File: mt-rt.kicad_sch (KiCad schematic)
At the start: 0 parts

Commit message: added MCU
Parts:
- added U?: nRF52820-QDxx, Package_DFN_QFN:QFN-40-1EP_5x5mm_P0.4mm_EP3.6x3.6mm, symbol MCU_Nordic:nRF52820-QDxx
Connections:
- new net: U?.37 (VSS), U?.41 (VSS)
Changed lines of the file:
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@@
 		(comment 2 "Copyright (c) 2025 MiraTherm")
+	)
+	(symbol
+		(lib_id "MCU_Nordic:nRF52820-QDxx")
+		(at 127 80.01 0)
+		(unit 1)
+		(exclude_from_sim no)
+		(in_bom yes)
+		(on_board yes)
+		(dnp no)
+		(fields_autoplaced yes)
+		(property "Reference" "U?"
+			(at 129.1433 105.41 0)
+			(effects
+				(font
+					(size 1.27 1.27)
+				)
+				(justify left)
+			)
+		)
+		(property "Value" "nRF52820-QDxx"
+			(at 129.1433 107.95 0)
+			(effects
+				(font
+					(size 1.27 1.27)
+				)
+				(justify left)
+			)
+		)
+		(property "Footprint" "Package_DFN_QFN:QFN-40-1EP_5x5mm_P0.4mm_EP3.6x3.6mm"
+			(at 127 115.57 0)
+			(effects
+				(font
+					(size 1.27 1.27)
+				)
+				(hide yes)
+			)
+		)
+		(property "Datasheet" "https://infocenter.nordicsemi.com/pdf/nRF52820_PS_v1.0.pdf"
+			(at 110.49 31.75 0)
+			(effects
+				(font
+					(size 1.27 1.27)
+				)
+				(hide yes)
+			)
+		)
+		(property "Description" "Multiprotocol BLE/ANT/2.4 GHz/802.15.4 Cortex-M4 SoC, QFN-40"
+			(at 127 80.01 0)
+			(effects
+				(font
+					(size 1.27 1.27)
+				)
+				(hide yes)
+			)
+		)
+		(pin "28"
+		)
+		(pin "29"
+		)
+		(pin "24"
+		)
+		(pin "21"
+		)
+		(pin "12"
+		)
+		(pin "22"
+		)
+		(pin "13"
+		)
+		(pin "16"
+		)
+		(pin "27"
+		)
+		(pin "26"
+		)
+		(pin "41"
+		)
+		(pin "39"
+		)
+		(pin "2"
+		)
+		(pin "37"
+		)
+		(pin "9"
+		)
+		(pin "36"
+		)
+		(pin "5"
+		)
+		(pin "6"
+		)
+		(pin "7"
+		)
+		(pin "14"
+		)
+		(pin "15"
+		)
+		(pin "38"
+		)
+		(pin "20"
+		)
+		(pin "1"
+		)
+		(pin "8"
+		)
+		(pin "3"
+		)
+		(pin "23"
+		)
+		(pin "17"
+		)
+		(pin "32"
+		)
+		(pin "4"
+		)
+		(pin "19"
+		)
+		(pin "18"
+		)
+		(pin "25"
+		)
+		(pin "35"
+		)
+		(pin "11"
+		)
+		(pin "30"
+		)
+		(pin "10"
+		)
+		(pin "40"
+		)
+		(pin "31"
+		)
+		(pin "34"
+		)
+		(pin "33"
+		)
+		(instances
+			(project ""
+				(path "/ee47f507-02e8-4ef5-a6d4-1ac4b2022b93"
+					(reference "U?")
+					(unit 1)
+				)
+			)
+		)
 	)
 	(sheet_instances

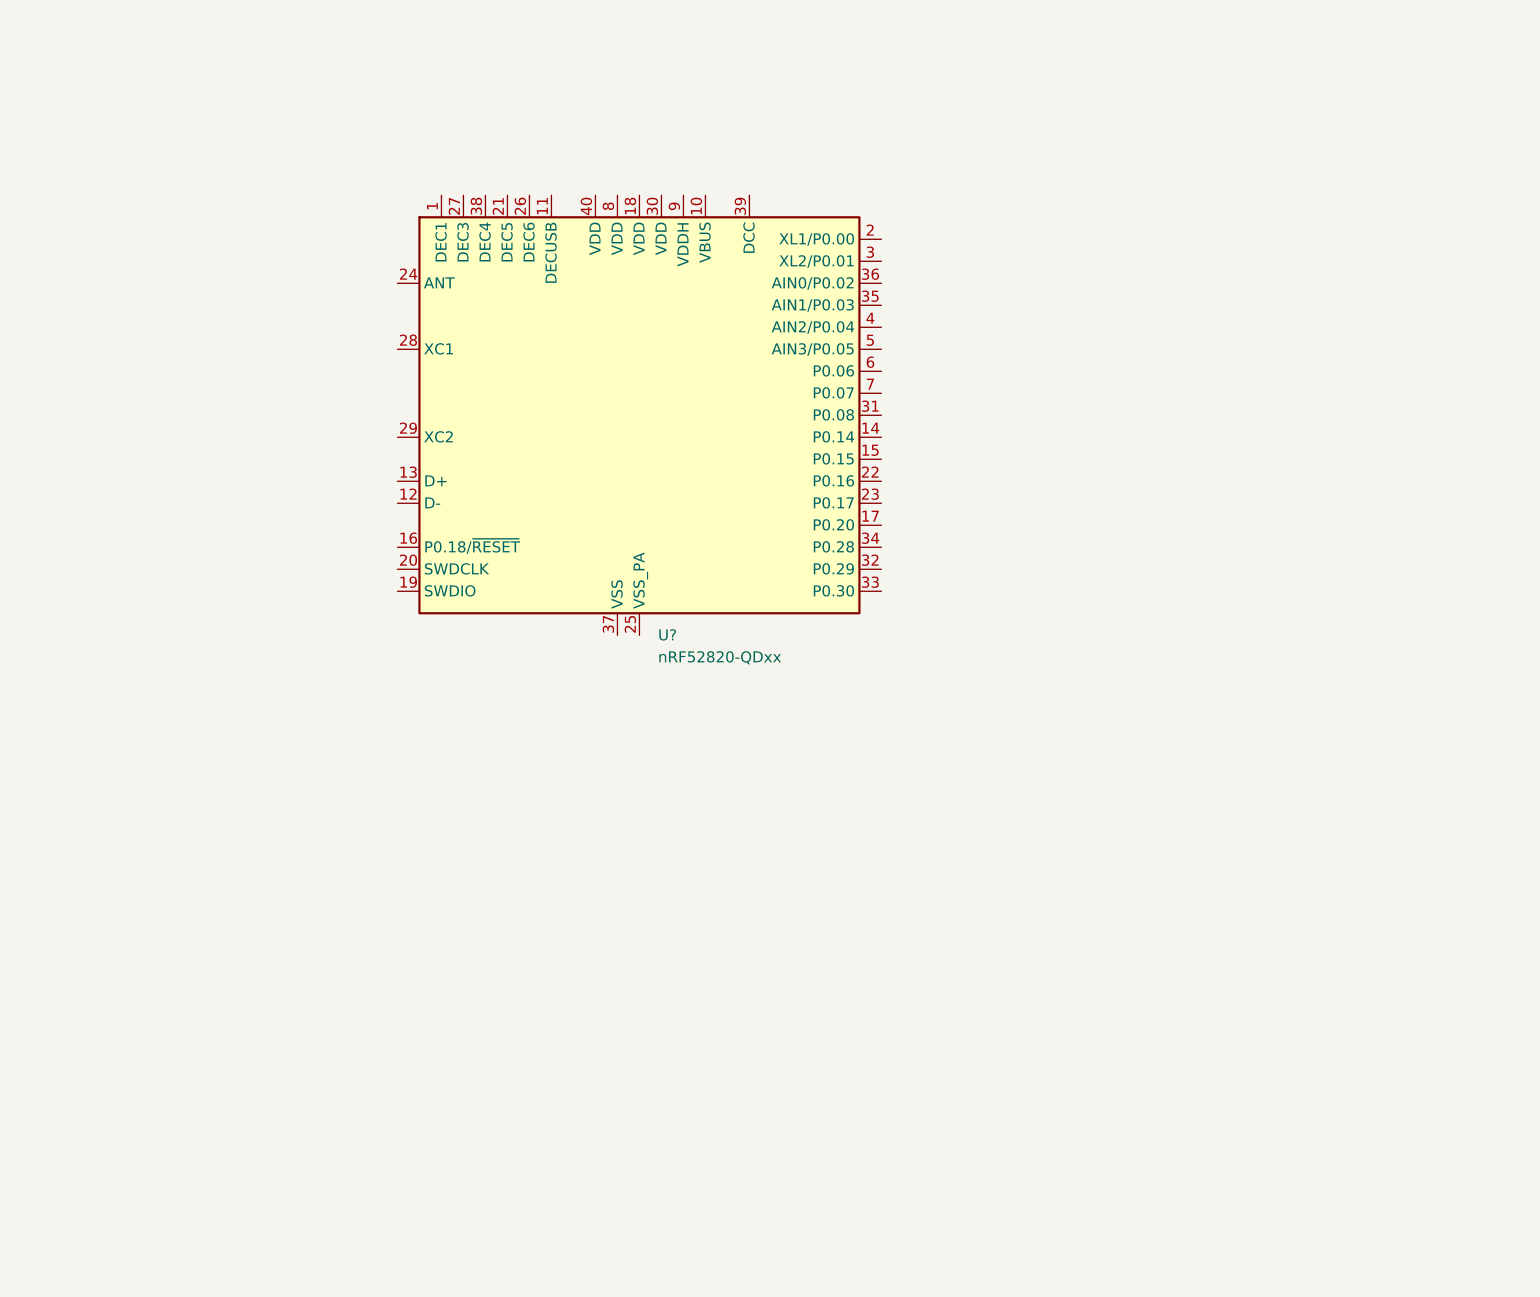
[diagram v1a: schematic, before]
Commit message: Added Rotary Encoder with switch
Added Custom Part Library
Added Encoder to Library
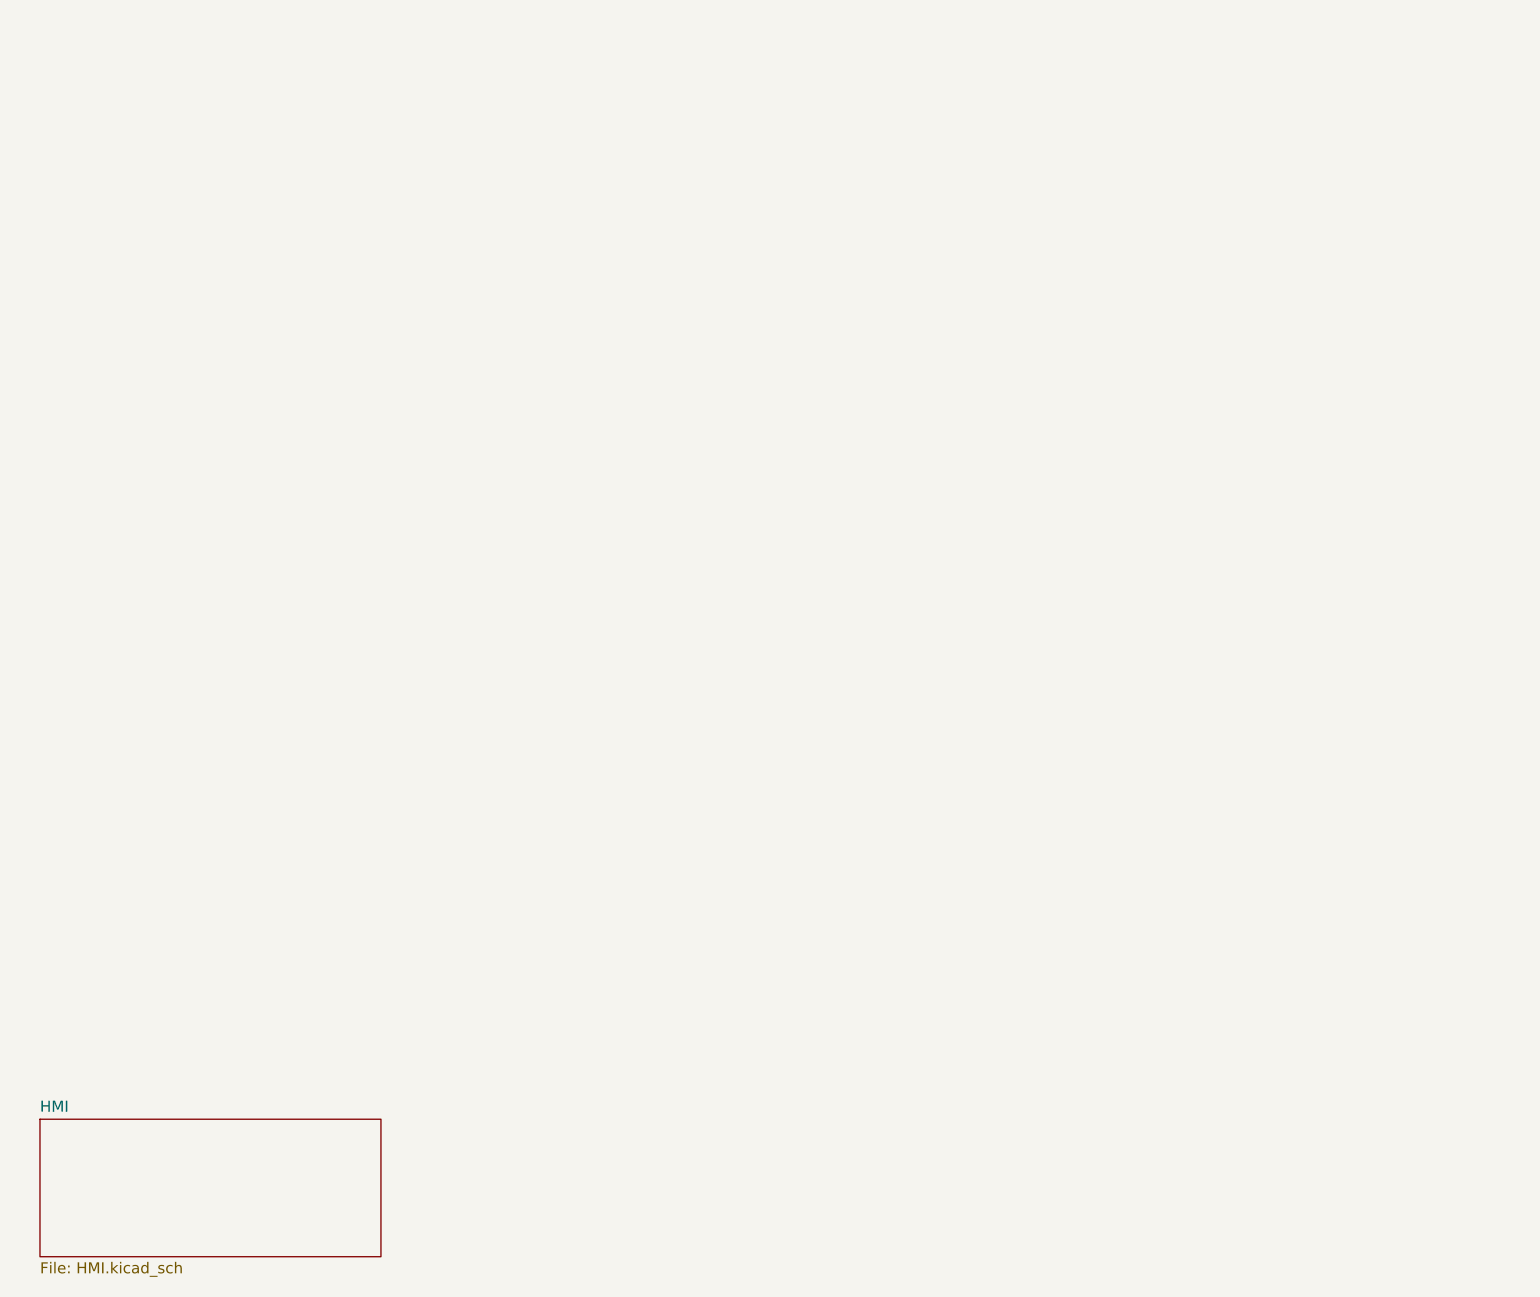
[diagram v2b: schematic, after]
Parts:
- removed U?: nRF52820-QDxx, Package_DFN_QFN:QFN-40-1EP_5x5mm_P0.4mm_EP3.6x3.6mm, symbol MCU_Nordic:nRF52820-QDxx
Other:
- added sheet HMI (HMI.kicad_sch)
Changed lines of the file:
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@@
 		(comment 2 "Copyright (c) 2025 MiraTherm")
 	)
-	(symbol
-		(lib_id "MCU_Nordic:nRF52820-QDxx")
-		(at 127 80.01 0)
-		(unit 1)
+	(sheet
+		(at 57.785 161.29)
+		(size 39.37 15.875)
 		(exclude_from_sim no)
 		(in_bom yes)
@@
 		(dnp no)
 		(fields_autoplaced yes)
-		(property "Reference" "U?"
-			(at 129.1433 105.41 0)
+		(stroke
+			(width 0.1524)
+			(type solid)
+		)
+		(fill
+			(color 0 0 0 0.0000)
+		)
+		(property "Sheetname" "HMI"
+			(at 57.785 160.5784 0)
 			(effects
 				(font
 					(size 1.27 1.27)
 				)
-				(justify left)
+				(justify left bottom)
 			)
 		)
-		(property "Value" "nRF52820-QDxx"
-			(at 129.1433 107.95 0)
+		(property "Sheetfile" "HMI.kicad_sch"
+			(at 57.785 177.7496 0)
 			(effects
 				(font
 					(size 1.27 1.27)
 				)
-				(justify left)
+				(justify left top)
 			)
 		)
-		(property "Footprint" "Package_DFN_QFN:QFN-40-1EP_5x5mm_P0.4mm_EP3.6x3.6mm"
-			(at 127 115.57 0)
-			(effects
-				(font
-					(size 1.27 1.27)
-				)
-				(hide yes)
-			)
-		)
-		(property "Datasheet" "https://infocenter.nordicsemi.com/pdf/nRF52820_PS_v1.0.pdf"
-			(at 110.49 31.75 0)
-			(effects
-				(font
-					(size 1.27 1.27)
-				)
-				(hide yes)
-			)
-		)
-		(property "Description" "Multiprotocol BLE/ANT/2.4 GHz/802.15.4 Cortex-M4 SoC, QFN-40"
-			(at 127 80.01 0)
-			(effects
-				(font
-					(size 1.27 1.27)
-				)
-				(hide yes)
-			)
-		)
-		(pin "28"
-		)
-		(pin "29"
-		)
-		(pin "24"
-		)
-		(pin "21"
-		)
-		(pin "12"
-		)
-		(pin "22"
-		)
-		(pin "13"
-		)
-		(pin "16"
-		)
-		(pin "27"
-		)
-		(pin "26"
-		)
-		(pin "41"
-		)
-		(pin "39"
-		)
-		(pin "2"
-		)
-		(pin "37"
-		)
-		(pin "9"
-		)
-		(pin "36"
-		)
-		(pin "5"
-		)
-		(pin "6"
-		)
-		(pin "7"
-		)
-		(pin "14"
-		)
-		(pin "15"
-		)
-		(pin "38"
-		)
-		(pin "20"
-		)
-		(pin "1"
-		)
-		(pin "8"
-		)
-		(pin "3"
-		)
-		(pin "23"
-		)
-		(pin "17"
-		)
-		(pin "32"
-		)
-		(pin "4"
-		)
-		(pin "19"
-		)
-		(pin "18"
-		)
-		(pin "25"
-		)
-		(pin "35"
-		)
-		(pin "11"
-		)
-		(pin "30"
-		)
-		(pin "10"
-		)
-		(pin "40"
-		)
-		(pin "31"
-		)
-		(pin "34"
-		)
-		(pin "33"
-		)
 		(instances
-			(project ""
+			(project "mt-rt"
 				(path "/ee47f507-02e8-4ef5-a6d4-1ac4b2022b93"
-					(reference "U?")
-					(unit 1)
+					(page "2")
 				)
 			)

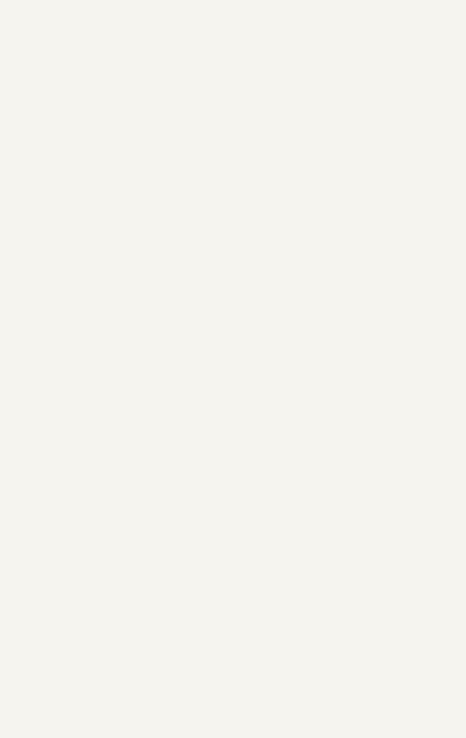
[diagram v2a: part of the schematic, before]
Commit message: added uC
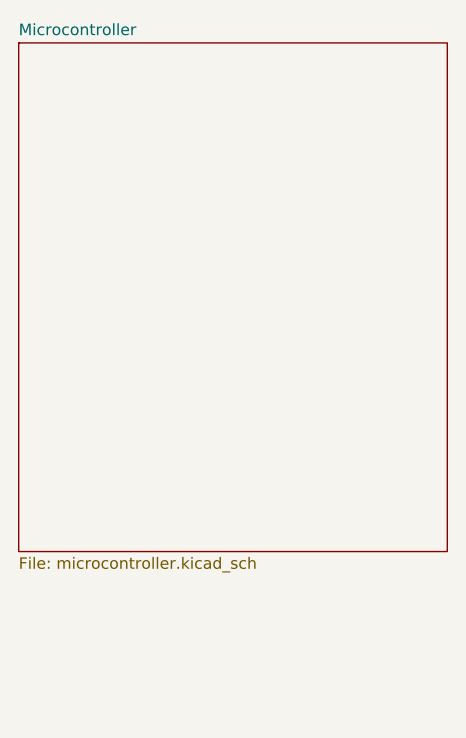
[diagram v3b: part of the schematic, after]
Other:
- added sheet Microcontroller (microcontroller.kicad_sch)
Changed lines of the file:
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@@
+		)
+	)
+	(sheet
+		(at 55.245 36.83)
+		(size 47.625 56.515)
+		(exclude_from_sim no)
+		(in_bom yes)
+		(on_board yes)
+		(dnp no)
+		(fields_autoplaced yes)
+		(stroke
+			(width 0.1524)
+			(type solid)
+		)
+		(fill
+			(color 0 0 0 0.0000)
+		)
+		(property "Sheetname" "Microcontroller"
+			(at 55.245 36.1184 0)
+			(effects
+				(font
+					(size 1.27 1.27)
+				)
+				(justify left bottom)
+			)
+		)
+		(property "Sheetfile" "microcontroller.kicad_sch"
+			(at 55.245 93.9296 0)
+			(effects
+				(font
+					(size 1.27 1.27)
+				)
+				(justify left top)
+			)
+		)
+		(instances
+			(project "mt-rt"
+				(path "/ee47f507-02e8-4ef5-a6d4-1ac4b2022b93"
+					(page "3")
+				)
+			)
 		)
 	)

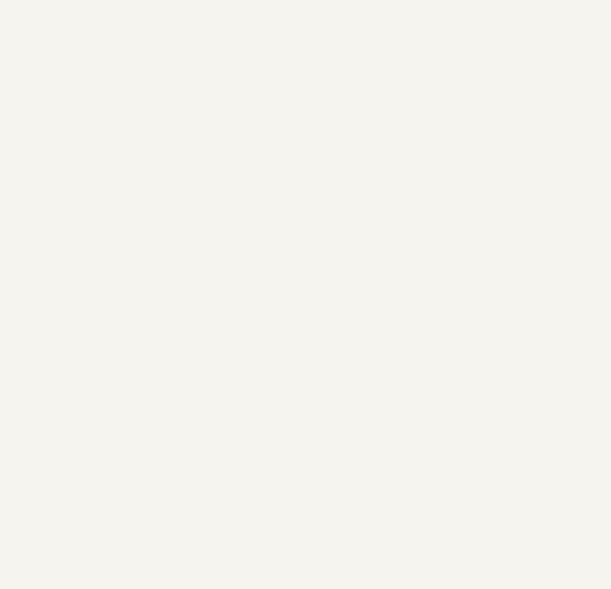
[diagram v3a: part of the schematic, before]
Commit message: Added Temperature Sensor
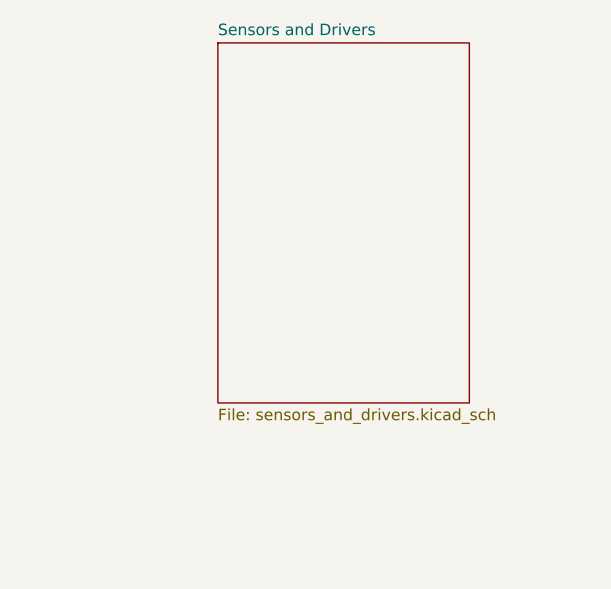
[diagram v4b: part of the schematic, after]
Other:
- added sheet Sensors and Drivers (sensors_and_drivers.kicad_sch)
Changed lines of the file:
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@@
+	)
+	(sheet
+		(at 187.325 36.83)
+		(size 27.94 40.005)
+		(exclude_from_sim no)
+		(in_bom yes)
+		(on_board yes)
+		(dnp no)
+		(fields_autoplaced yes)
+		(stroke
+			(width 0.1524)
+			(type solid)
+		)
+		(fill
+			(color 0 0 0 0.0000)
+		)
+		(property "Sheetname" "Sensors and Drivers"
+			(at 187.325 36.1184 0)
+			(effects
+				(font
+					(size 1.27 1.27)
+				)
+				(justify left bottom)
+			)
+		)
+		(property "Sheetfile" "sensors_and_drivers.kicad_sch"
+			(at 187.325 77.4196 0)
+			(effects
+				(font
+					(size 1.27 1.27)
+				)
+				(justify left top)
+			)
+		)
+		(instances
+			(project "mt-rt"
+				(path "/ee47f507-02e8-4ef5-a6d4-1ac4b2022b93"
+					(page "4")
+				)
+			)
+		)
 	)
 	(sheet
